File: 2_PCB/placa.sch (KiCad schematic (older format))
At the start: 41 parts, among them J1 Screw_Terminal_01x02, J2 Conn_01x04_Male, J3 Screw_Terminal_01x02, J4 TestPoints, J5 Conn_01x02_Male, U1 STM32L051C8Tx, U2 Ai-Thinker-Ra-01, Y1 8 MHz, Y2 32.768 kHz

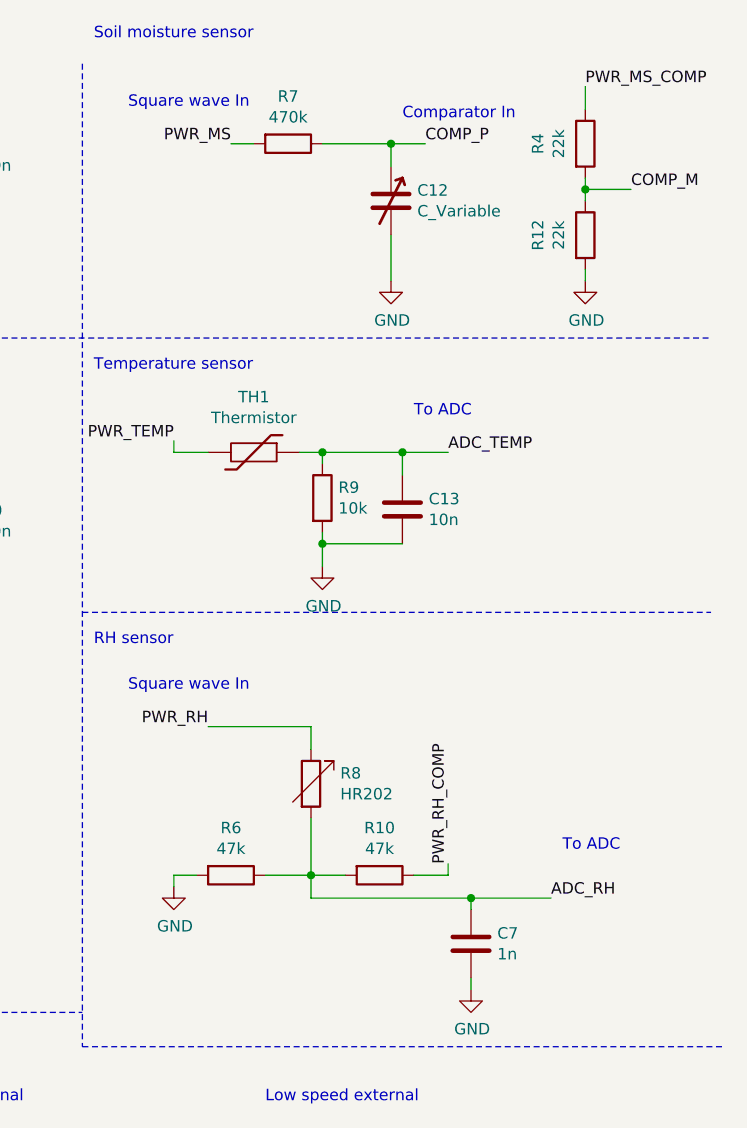
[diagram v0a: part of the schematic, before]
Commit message: Hardware tested all. MS, HR202, Temperature and LoRa module. Added code for the gateway
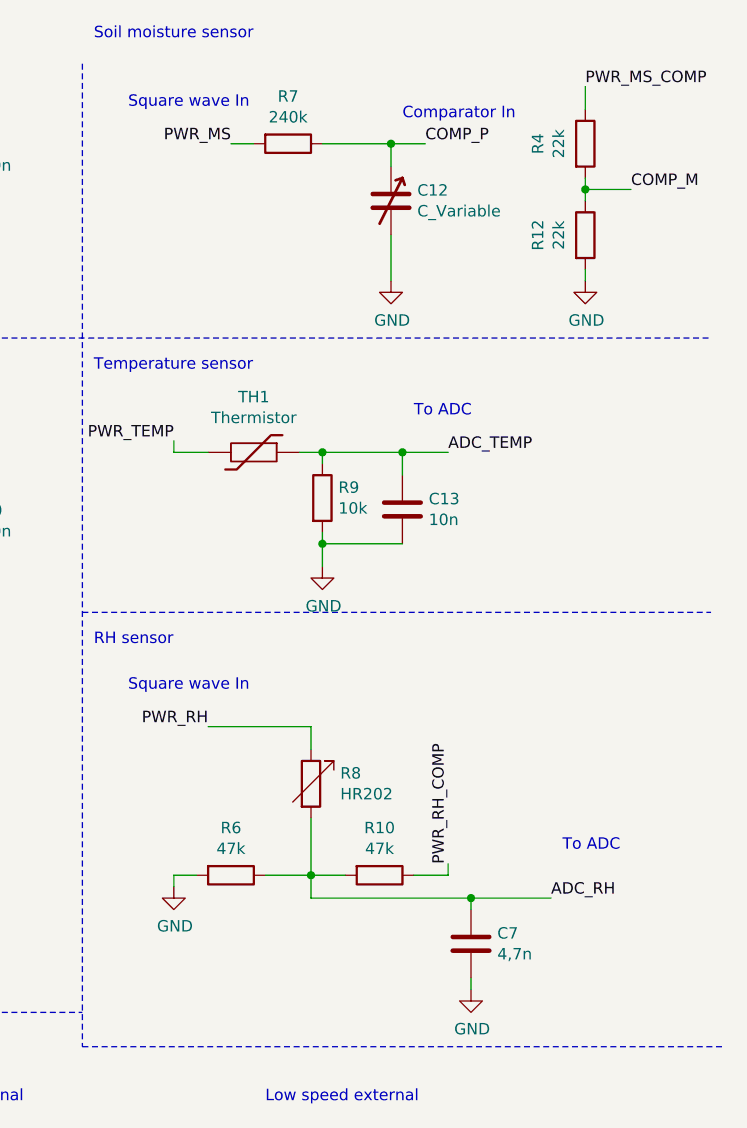
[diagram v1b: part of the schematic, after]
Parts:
- C7: value 1n -> 4,7n
- R7: value 470k -> 240k
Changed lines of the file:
@@
 encoding utf-8
 Sheet 1 1
-Title ""
-Date ""
+Title "IoT Soil Sensor"
+Date "2018-11-21"
 Rev ""
 Comp ""
@@
 P 9350 1050
 F 0 "R7" V 9143 1050 50  0000 C CNN
-F 1 "470k" V 9234 1050 50  0000 C CNN
+F 1 "240k" V 9234 1050 50  0000 C CNN
 F 2 "Resistor_SMD:R_0805_2012Metric_Pad1.15x1.40mm_HandSolder" V 9280 1050 50  0001 C CNN
 F 3 "~" H 9350 1050 50  0001 C CNN
@@
 P 10150 4550
 F 0 "C7" H 10265 4596 50  0000 L CNN
-F 1 "1n" H 10265 4505 50  0000 L CNN
+F 1 "4,7n" H 10265 4505 50  0000 L CNN
 F 2 "Capacitor_SMD:C_0805_2012Metric_Pad1.15x1.40mm_HandSolder" H 10188 4400 50  0001 C CNN
 F 3 "~" H 10150 4550 50  0001 C CNN

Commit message: Cleaned repo and organized it
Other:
- note added: "Decoupling caps"
- note added: "Test points for the SPI LoRa connection"
- moved on the sheet: C1, J2, J5
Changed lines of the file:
@@
 	1    0    0    -1
 $EndComp
-Text Notes 6000 650  0    50   ~ 0
+Text Notes 5650 650  0    50   ~ 0
 Power Supply
 Text Notes 550  6450 0    50   ~ 0
@@
 L power:GND #PWR0109
 U 1 1 5B8D5FED
-P 1450 7650
-F 0 "#PWR0109" H 1450 7400 50  0001 C CNN
-F 1 "GND" H 1455 7477 50  0000 C CNN
-F 2 "" H 1450 7650 50  0001 C CNN
-F 3 "" H 1450 7650 50  0001 C CNN
-	1    1450 7650
+P 1700 7400
+F 0 "#PWR0109" H 1700 7150 50  0001 C CNN
+F 1 "GND" H 1705 7227 50  0000 C CNN
+F 2 "" H 1700 7400 50  0001 C CNN
+F 3 "" H 1700 7400 50  0001 C CNN
+	1    1700 7400
 	1    0    0    -1
 $EndComp
@@
 Wire Wire Line
 	3650 4800 3450 4800
-Text Label 900  7000 0    50   ~ 0
+Text Label 1150 6750 0    50   ~ 0
 SWCLK
-Text Label 900  7300 0    50   ~ 0
+Text Label 1150 7050 0    50   ~ 0
 SWDIO
-Text Label 1000 7550 0    50   ~ 0
+Text Label 1250 7300 0    50   ~ 0
 NRST
 $Comp
 L power:VCC #PWR0110
 U 1 1 5B8DD502
-P 1450 7200
-F 0 "#PWR0110" H 1450 7050 50  0001 C CNN
-F 1 "VCC" H 1467 7373 50  0000 C CNN
-F 2 "" H 1450 7200 50  0001 C CNN
-F 3 "" H 1450 7200 50  0001 C CNN
-	1    1450 7200
+P 1700 6950
+F 0 "#PWR0110" H 1700 6800 50  0001 C CNN
+F 1 "VCC" H 1717 7123 50  0000 C CNN
+F 2 "" H 1700 6950 50  0001 C CNN
+F 3 "" H 1700 6950 50  0001 C CNN
+	1    1700 6950
 	1    0    0    -1
 $EndComp
@@
 L Device:C C1
 U 1 1 5B8E21D1
-P 1450 7450
-F 0 "C1" H 1565 7496 50  0000 L CNN
-F 1 "100n" H 1565 7405 50  0000 L CNN
-F 2 "Capacitor_SMD:C_0805_2012Metric_Pad1.15x1.40mm_HandSolder" H 1488 7300 50  0001 C CNN
-F 3 "~" H 1450 7450 50  0001 C CNN
-	1    1450 7450
+P 1700 7200
+F 0 "C1" H 1815 7246 50  0000 L CNN
+F 1 "100n" H 1815 7155 50  0000 L CNN
+F 2 "Capacitor_SMD:C_0805_2012Metric_Pad1.15x1.40mm_HandSolder" H 1738 7050 50  0001 C CNN
+F 3 "~" H 1700 7200 50  0001 C CNN
+	1    1700 7200
 	1    0    0    -1
 $EndComp
@@
 	10150 4400 10150 4350
 Connection ~ 10150 4350
-Wire Notes Line
-	8450 700  8450 5000
 Wire Wire Line
 	9850 2800 9500 2800
@@
 Text Label 8650 5450 0    50   ~ 0
 RCC_OSC_OUT
-Text Notes 7000 5000 0    50   ~ 0
+Text Notes 7000 5150 0    50   ~ 0
 Oscillators
-Wire Notes Line
-	6950 4850 6950 7800
 Wire Notes Line
 	6750 7800 6800 7800
@@
 	8650 5950 8650 5900
 Connection ~ 8650 5900
-Wire Notes Line
-	8450 5000 11250 5000
 Text Notes 9250 5250 0    50   ~ 0
 Low speed external
@@
 Wire Wire Line
 	3450 3900 3650 3900
-Text Notes 5800 2100 0    50   ~ 0
+Text Notes 5650 2100 0    50   ~ 0
 LoRa RA-01
 Wire Wire Line
@@
 Text Notes 1100 1500 0    50   ~ 0
 Microcontroller
-Wire Notes Line
-	5200 500  5200 4850
 Wire Wire Line
 	3650 4500 3450 4500
@@
 Wire Notes Line
 	5200 1900 11200 1900
-Wire Notes Line
-	5200 4850 8450 4850
 $Comp
 L Connector:Conn_01x04_Female J4
@@
 L Connector:Conn_01x04_Male J2
 U 1 1 5BB700CF
-P 650 7100
-F 0 "J2" H 756 7378 50  0000 C CNN
-F 1 "Conn_01x04_Male" H 756 7287 50  0000 C CNN
-F 2 "Connector_PinHeader_2.54mm:PinHeader_1x04_P2.54mm_Vertical" H 650 7100 50  0001 C CNN
-F 3 "~" H 650 7100 50  0001 C CNN
-	1    650  7100
+P 900 6850
+F 0 "J2" H 1006 7128 50  0000 C CNN
+F 1 "Conn_01x04_Male" H 1006 7037 50  0000 C CNN
+F 2 "Connector_PinHeader_2.54mm:PinHeader_1x04_P2.54mm_Vertical" H 900 6850 50  0001 C CNN
+F 3 "~" H 900 6850 50  0001 C CNN
+	1    900  6850
 	1    0    0    -1
 $EndComp
@@
 L power:GND #PWR0106
 U 1 1 5BB95E51
-P 950 7100
-F 0 "#PWR0106" H 950 6850 50  0001 C CNN
-F 1 "GND" H 955 6927 50  0000 C CNN
-F 2 "" H 950 7100 50  0001 C CNN
-F 3 "" H 950 7100 50  0001 C CNN
-	1    950  7100
+P 1200 6850
+F 0 "#PWR0106" H 1200 6600 50  0001 C CNN
+F 1 "GND" H 1205 6677 50  0000 C CNN
+F 2 "" H 1200 6850 50  0001 C CNN
+F 3 "" H 1200 6850 50  0001 C CNN
+	1    1200 6850
 	0    -1   -1   0
 $EndComp
 Wire Wire Line
-	900  7300 850  7300
-Wire Wire Line
-	900  7000 850  7000
-Wire Wire Line
-	1450 7650 1450 7600
+	1150 7050 1100 7050
+Wire Wire Line
+	1150 6750 1100 6750
+Wire Wire Line
+	1700 7400 1700 7350
 Wire Wire Line
 	3000 7350 3000 7600
@@
 L Connector:Conn_01x02_Male J5
 U 1 1 5BBE81FC
-P 600 7550
-F 0 "J5" H 706 7728 50  0000 C CNN
-F 1 "Conn_01x02_Male" H 706 7637 50  0000 C CNN
-F 2 "Connector_PinHeader_2.54mm:PinHeader_1x02_P2.54mm_Vertical" H 600 7550 50  0001 C CNN
-F 3 "~" H 600 7550 50  0001 C CNN
-	1    600  7550
+P 850 7300
+F 0 "J5" H 956 7478 50  0000 C CNN
+F 1 "Conn_01x02_Male" H 956 7387 50  0000 C CNN
+F 2 "Connector_PinHeader_2.54mm:PinHeader_1x02_P2.54mm_Vertical" H 850 7300 50  0001 C CNN
+F 3 "~" H 850 7300 50  0001 C CNN
+	1    850  7300
 	1    0    0    -1
 $EndComp
@@
 L power:GND #PWR0124
 U 1 1 5BBF1F50
-P 900 7700
-F 0 "#PWR0124" H 900 7450 50  0001 C CNN
-F 1 "GND" H 905 7527 50  0000 C CNN
-F 2 "" H 900 7700 50  0001 C CNN
-F 3 "" H 900 7700 50  0001 C CNN
-	1    900  7700
-	1    0    0    -1
-$EndComp
-Wire Wire Line
-	800  7550 1000 7550
-Wire Wire Line
-	800  7650 900  7650
-Wire Wire Line
-	900  7650 900  7700
-Wire Wire Line
-	1450 7200 1450 7300
-Wire Wire Line
-	850  7200 1450 7200
-Connection ~ 1450 7200
-Wire Wire Line
-	950  7100 850  7100
+P 1150 7450
+F 0 "#PWR0124" H 1150 7200 50  0001 C CNN
+F 1 "GND" H 1155 7277 50  0000 C CNN
+F 2 "" H 1150 7450 50  0001 C CNN
+F 3 "" H 1150 7450 50  0001 C CNN
+	1    1150 7450
+	1    0    0    -1
+$EndComp
+Wire Wire Line
+	1050 7300 1250 7300
+Wire Wire Line
+	1050 7400 1150 7400
+Wire Wire Line
+	1150 7400 1150 7450
+Wire Wire Line
+	1700 6950 1700 7050
+Wire Wire Line
+	1100 6950 1700 6950
+Connection ~ 1700 6950
+Wire Wire Line
+	1200 6850 1100 6850
 Wire Wire Line
 	6100 3400 6250 3400
@@
 	2150 4500 2250 4500
 NoConn ~ 2250 4700
+Text Notes 3900 2100 0    50   ~ 0
+Decoupling caps
+Text Notes 5300 4200 0    31   ~ 0
+Test points for the SPI LoRa connection
+Wire Notes Line
+	5200 500  5200 5000
+Wire Notes Line
+	6950 6550 6950 5000
+Wire Notes Line
+	5200 5000 11250 5000
+Wire Notes Line
+	8450 450  8450 5000
 $EndSCHEMATC
